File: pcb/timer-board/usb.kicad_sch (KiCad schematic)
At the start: 7 parts, among them J1 USB-C_USB-310F-B-SU

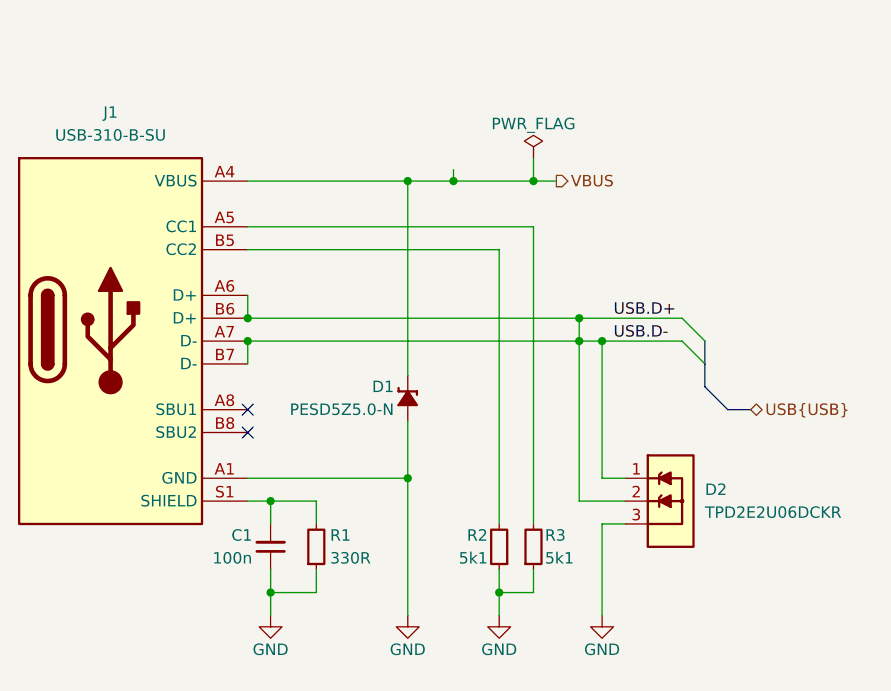
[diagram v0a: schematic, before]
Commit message: Connect OLED display, position main components
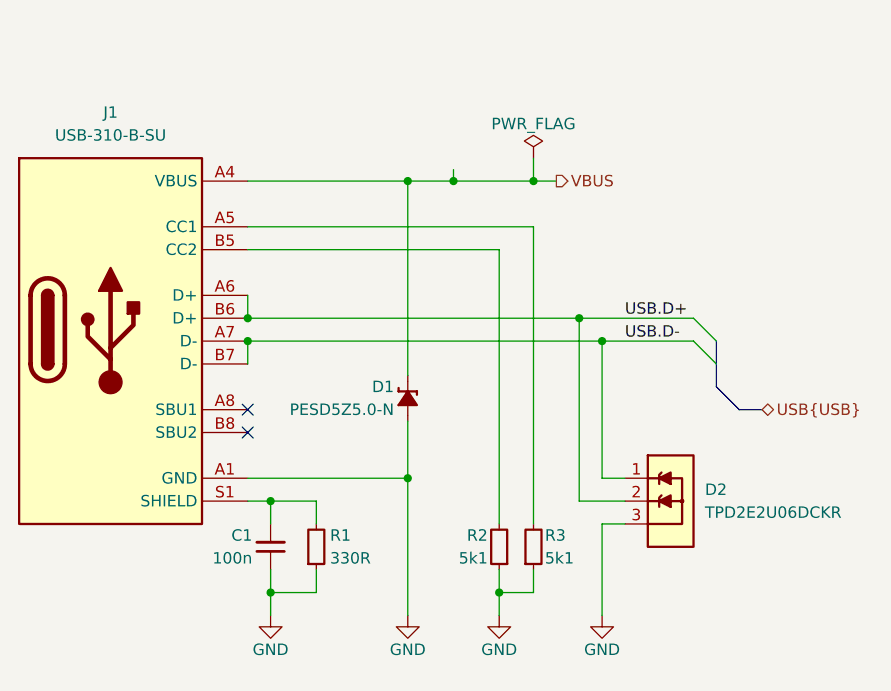
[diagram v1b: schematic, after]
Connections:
- net USB.D+: no longer D2.1, J1.A7 (D-), J1.B7 (D-)
- new net USB.D-: D2.1, J1.A7 (D-), J1.B7 (D-)
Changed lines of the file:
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@@
-	)
-	(junction
-		(at 160.02 93.98)
-		(diameter 0)
-		(color 0 0 0 0)
 	)
 	(junction
@@
 	)
 	(bus_entry
-		(at 173.99 96.52)
+		(at 175.26 96.52)
 		(size -2.54 -2.54)
 		(stroke
@@
 	)
 	(bus_entry
-		(at 173.99 93.98)
+		(at 175.26 93.98)
 		(size -2.54 -2.54)
 		(stroke
@@
 	(bus
 		(pts
-			(xy 176.53 101.6) (xy 173.99 99.06)
+			(xy 177.8 101.6) (xy 175.26 99.06)
 		)
 		(stroke
@@
 	(wire
 		(pts
-			(xy 160.02 91.44) (xy 160.02 93.98)
+			(xy 160.02 91.44) (xy 160.02 111.76)
 		)
 		(stroke
@@
 	(wire
 		(pts
+			(xy 162.56 93.98) (xy 172.72 93.98)
+		)
+		(stroke
+			(width 0)
+			(type default)
+		)
+	)
+	(wire
+		(pts
 			(xy 154.94 73.66) (xy 154.94 76.2)
 		)
@@
 	(wire
 		(pts
-			(xy 160.02 91.44) (xy 171.45 91.44)
-		)
-		(stroke
-			(width 0)
-			(type default)
-		)
-	)
-	(wire
-		(pts
 			(xy 157.48 76.2) (xy 154.94 76.2)
 		)
@@
 	(wire
 		(pts
-			(xy 160.02 93.98) (xy 160.02 111.76)
-		)
-		(stroke
-			(width 0)
-			(type default)
-		)
-	)
-	(wire
-		(pts
 			(xy 140.97 76.2) (xy 146.05 76.2)
 		)
@@
 	(wire
 		(pts
-			(xy 162.56 93.98) (xy 160.02 93.98)
-		)
-		(stroke
-			(width 0)
-			(type default)
-		)
-	)
-	(wire
-		(pts
 			(xy 146.05 76.2) (xy 154.94 76.2)
 		)
@@
 	(bus
 		(pts
-			(xy 179.07 101.6) (xy 176.53 101.6)
+			(xy 180.34 101.6) (xy 177.8 101.6)
 		)
 		(stroke
@@
 	(bus
 		(pts
-			(xy 173.99 96.52) (xy 173.99 99.06)
-		)
-		(stroke
-			(width 0)
-			(type default)
-		)
-	)
-	(wire
-		(pts
-			(xy 123.19 93.98) (xy 160.02 93.98)
+			(xy 175.26 96.52) (xy 175.26 99.06)
+		)
+		(stroke
+			(width 0)
+			(type default)
+		)
+	)
+	(wire
+		(pts
+			(xy 123.19 93.98) (xy 162.56 93.98)
 		)
 		(stroke
@@
 		)
 	)
+	(wire
+		(pts
+			(xy 160.02 91.44) (xy 172.72 91.44)
+		)
+		(stroke
+			(width 0)
+			(type default)
+		)
+	)
 	(bus
 		(pts
-			(xy 173.99 93.98) (xy 173.99 96.52)
+			(xy 175.26 93.98) (xy 175.26 96.52)
 		)
 		(stroke
@@
 	(wire
 		(pts
-			(xy 162.56 93.98) (xy 171.45 93.98)
-		)
-		(stroke
-			(width 0)
-			(type default)
-		)
-	)
-	(wire
-		(pts
 			(xy 130.81 121.92) (xy 125.73 121.92)
 		)
@@
 	)
 	(label "USB.D-"
-		(at 163.83 93.98 0)
+		(at 165.1 93.98 0)
 		(effects
 			(font
@@
 	)
 	(label "USB.D+"
-		(at 163.83 91.44 0)
+		(at 165.1 91.44 0)
 		(effects
 			(font
@@
 	(hierarchical_label "USB{USB}"
 		(shape bidirectional)
-		(at 179.07 101.6 0)
+		(at 180.34 101.6 0)
 		(effects
 			(font
@@
 		)
 	)
+	(rule_area
+		(polyline
+			(pts
+				(xy 163.83 104.14) (xy 191.77 104.14) (xy 191.77 87.63) (xy 163.83 87.63)
+			)
+			(stroke
+				(width 0)
+				(type dash)
+			)
+			(fill
+				(type none)
+			)
+		)
+	)
+	(netclass_flag ""
+		(length 2.54)
+		(shape round)
+		(at 191.77 87.63 0)
+		(fields_autoplaced yes)
+		(effects
+			(font
+				(size 1.27 1.27)
+			)
+			(justify left bottom)
+		)
+		(property "Netclass" "USB_90Ohm_diff"
+			(at 191.0715 85.09 0)
+			(effects
+				(font
+					(size 1.27 1.27)
+				)
+				(justify right)
+			)
+		)
+		(property "Component Class" ""
+			(at -21.59 -5.08 0)
+			(effects
+				(font
+					(size 1.27 1.27)
+					(italic yes)
+				)
+				(justify right)
+			)
+		)
+	)

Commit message: Finish uncompleted schematic sections, layout most of the PCB
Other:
- note added: "USB-C"
- moved on the sheet: C1, D1, D2, J1, R1, R2, R3

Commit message: Add I2C pull-up, IR receiver decoupling, LED labels, clear ERC and DRC
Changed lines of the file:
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@@
+		)
+	)
+	(wire
+		(pts
+			(xy 179.07 123.19) (xy 179.07 125.73)
+		)
+		(stroke
+			(width 0)
+			(type default)
 		)
 	)
@@
 					(size 1.27 1.27)
 					(italic yes)
+				)
+			)
+		)
+	)
+	(symbol
+		(lib_id "DW-power-symbols:GND")
+		(at 179.07 125.73 0)
+		(mirror y)
+		(unit 1)
+		(exclude_from_sim no)
+		(in_bom yes)
+		(on_board yes)
+		(dnp no)
+		(property "Reference" "#PWR042"
+			(at 179.07 132.08 0)
+			(effects
+				(font
+					(size 1.27 1.27)
+				)
+				(hide yes)
+			)
+		)
+		(property "Value" "GND"
+			(at 179.07 129.54 0)
+			(effects
+				(font
+					(size 1.27 1.27)
+				)
+			)
+		)
+		(property "Footprint" ""
+			(at 179.07 125.73 0)
+			(effects
+				(font
+					(size 1.27 1.27)
+				)
+				(hide yes)
+			)
+		)
+		(property "Datasheet" ""
+			(at 179.07 125.73 0)
+			(effects
+				(font
+					(size 1.27 1.27)
+				)
+				(hide yes)
+			)
+		)
+		(property "Description" "Power symbol creates a global label with name \"GND\" , ground"
+			(at 179.07 125.73 0)
+			(effects
+				(font
+					(size 1.27 1.27)
+				)
+				(hide yes)
+			)
+		)
+		(pin "1"
+		)
+		(instances
+			(project "timer-board"
+				(path "/c6951331-127b-46f8-97b9-b4f2222f059c/8fcb1262-e980-4c4d-ae95-df63a5738347"
+					(reference "#PWR042")
+					(unit 1)
 				)
 			)
@@
 					(unit 1)
 				)
+			)
+		)
+	)
+	(symbol
+		(lib_id "DW-power-symbols:PWR_FLAG")
+		(at 179.07 123.19 0)
+		(unit 1)
+		(exclude_from_sim no)
+		(in_bom yes)
+		(on_board yes)
+		(dnp no)
+		(property "Reference" "#FLG02"
+			(at 179.07 121.285 0)
+			(effects
+				(font
+					(size 1.27 1.27)
+				)
+				(hide yes)
+			)
+		)
+		(property "Value" "PWR_FLAG"
+			(at 179.07 119.38 0)
+			(effects
+				(font
+					(size 1.27 1.27)
+				)
+			)
+		)
+		(property "Footprint" ""
+			(at 179.07 123.19 0)
+			(effects
+				(font
+					(size 1.27 1.27)
+				)
+				(hide yes)
+			)
+		)
+		(property "Datasheet" "~"
+			(at 179.07 123.19 0)
+			(effects
+				(font
+					(size 1.27 1.27)
+				)
+				(hide yes)
+			)
+		)
+		(property "Description" "Special symbol for telling ERC where power comes from"
+			(at 179.07 123.19 0)
+			(effects
+				(font
+					(size 1.27 1.27)
+				)
+				(hide yes)
+			)
+		)
+		(pin "1"
+		)
+		(instances
+			(project "timer-board"
+				(path "/c6951331-127b-46f8-97b9-b4f2222f059c/8fcb1262-e980-4c4d-ae95-df63a5738347"
+					(reference "#FLG02")
+					(unit 1)
+				)
